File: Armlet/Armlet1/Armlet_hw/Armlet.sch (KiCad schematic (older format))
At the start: 65 parts, among them Q1 NPN, SW1 BUTTON

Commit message: 
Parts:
- removed B? (x3): BAT, symbol BAT
- removed C6: 3.3pF, symbol C
- removed C? (x2): 0.1u, symbol C
- removed C? (x2): 10u, symbol C
- removed D?: D_SHOTTKY, symbol D_SHOTTKY
- removed DA?: NCP1400, symbol NCP1400
- removed DD2: STM32F10X-48, symbol STM32F10X-48
- removed FU?: SOLDERFUSE, symbol SOLDERFUSE
- removed L2, L3, L6, L7: 12nH, 0402, symbol L
- removed L4, L5: 18nH, 0402, symbol L
- removed L?: 22uH, symbol L
- removed R25: 10k, symbol R
- removed RP1, RP2: REFPOINT, symbol REFPOINT
- removed TP2, TP3, TP4: TESTPOINT, symbol TESTPOINT
- removed XL?: CONN_10, symbol CONN_10
- removed XL?: CONN_1, symbol CONN_1
- removed XTAL2: 27MHz, symbol CRYSTAL
- added B1: BAT, BAT_LP383450, symbol BAT
- added C17, C26: 0.1u, symbol C
- added C22, C23: 10u, symbol C
- added C24: 10u, CAP_0805, symbol C
- added C25: 0.1u, CAP_0603, symbol C
- added C27, C28, C29: 1u, symbol C
- added C4: 1.5pF, symbol C
- added D1: 1N4148, SOD323, symbol DIODE
- added DA1: BQ24010, symbol BQ24010
- added DA2: AAT3221, symbol AAT3221
- added DA3: NCP662SQ, symbol NCP662SQ
- added DD2: STM32F100C4, symbol STM32F100C4
- added DD3: M24C02, TSSOP8, symbol EEPROM_I2C
- added R10: 1.5k, symbol R
- added R6: 1.8k*, symbol R
- added R7, R9: 100k, symbol R
- added R8: 3.9k*, symbol R
- added TP1: TESTPOINT, symbol TESTPOINT
- added XL4: USB_MINI_B, symbol USB_MINI_B
- added XTAL1: 26MHz, CRYSTAL, symbol CRYSTAL_H
- C12: renamed from C15; value 18pF -> 10pF
- C13: renamed from C16; value 18pF -> 10pF
- C18: value 0.1u -> 4.7u
- C5: value 1.5pF -> 3.3pF
- gave numbers to parts that had none: 12
- renumbered C12 to C10, C13 to C11, C17 to C14, C4 to C15, C14 to C16, C20 to C19, C8 to C6, C9 to C7, C10 to C8, C11 to C9, Q1 to Q2, R7 to R5, TP5 to TP2, TP1 to TP3
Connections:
- net labels added: +5V, CC_GDO2, CHRG, CHRG_DONE, PB0, PB1, PWR_GOOD, UBat/2
- net labels removed: ADC_BAT, BatteryBtw, Lout, PA12, PB0T3C3, PB1T3C4, PB8, PB9, RX2, TX2
- wire segments 196 -> 229
- no-connect marks 8 -> 9
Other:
- note added: "3.3V 150mA power regulator"
- note added: "I2C Addr = 1010 (A2)(A1)(A0) = 1010 111"
- note added: "L 12nH"
- note added: "L 18nH"
- note added: "Li-Ion charger\n1.5k => 0.56 A"
- note added: "Power"
- note removed: "Solder the fuse \nif no battery installed"
- moved on the sheet: BZ1, C15, C16, C20, C21, M1, Q1, Q2, R2, R3, R4, R5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

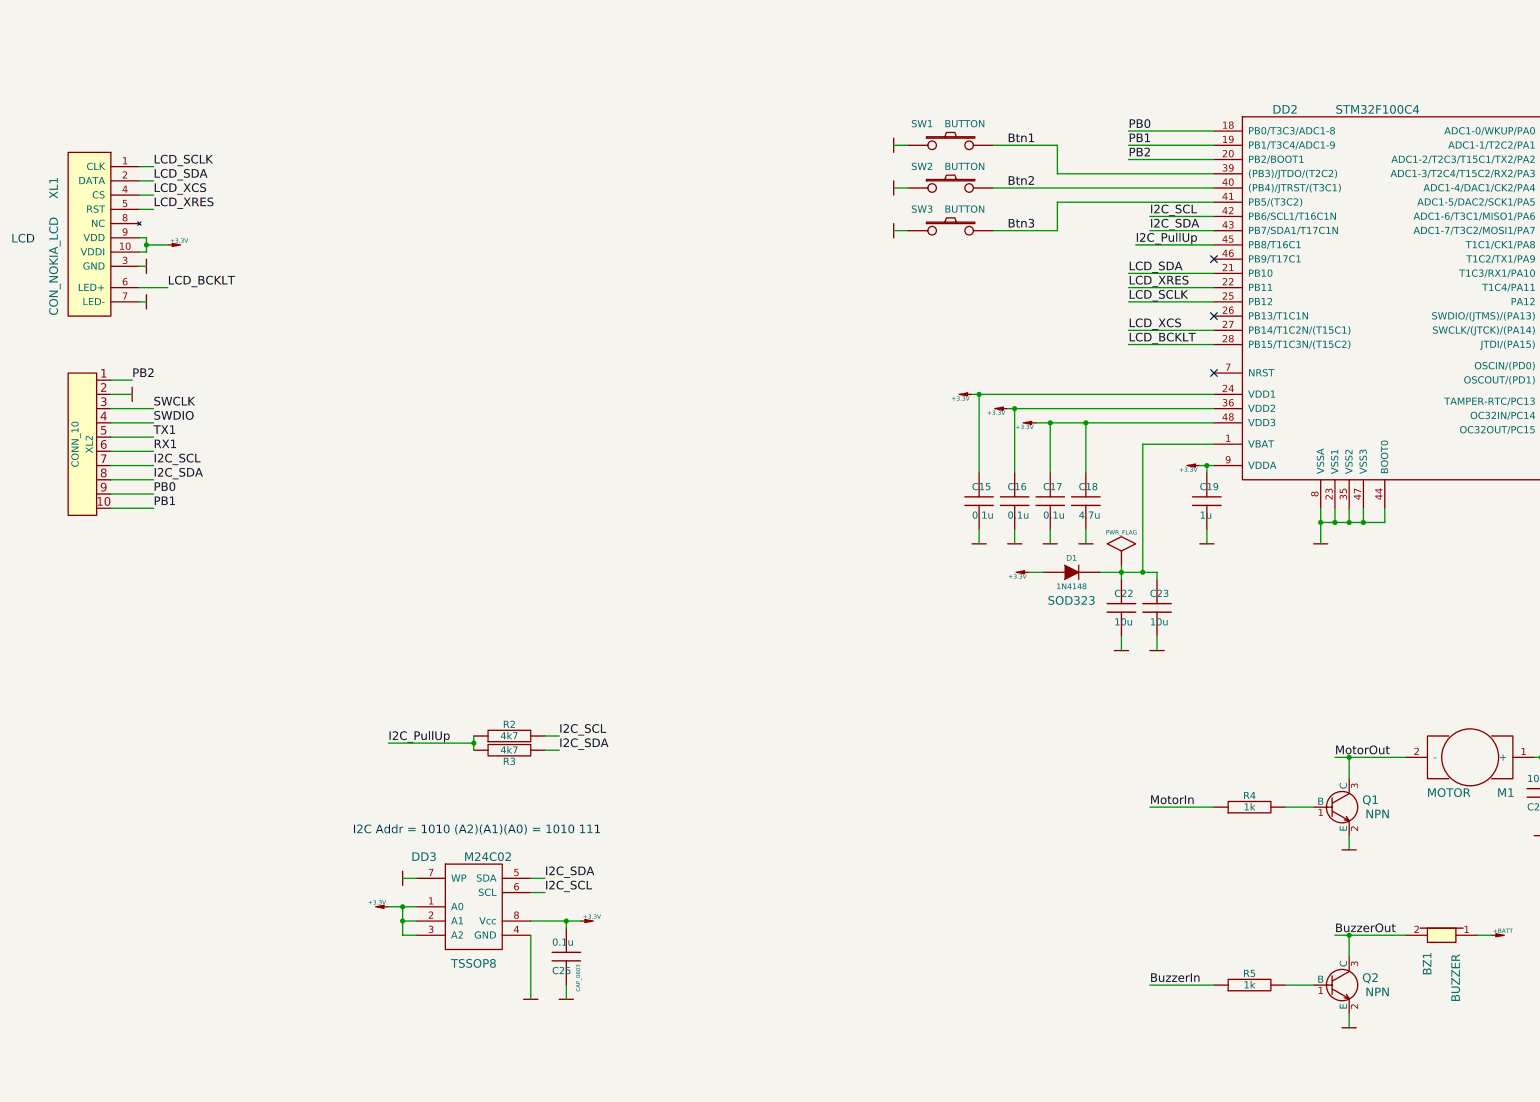
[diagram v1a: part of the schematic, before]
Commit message: 
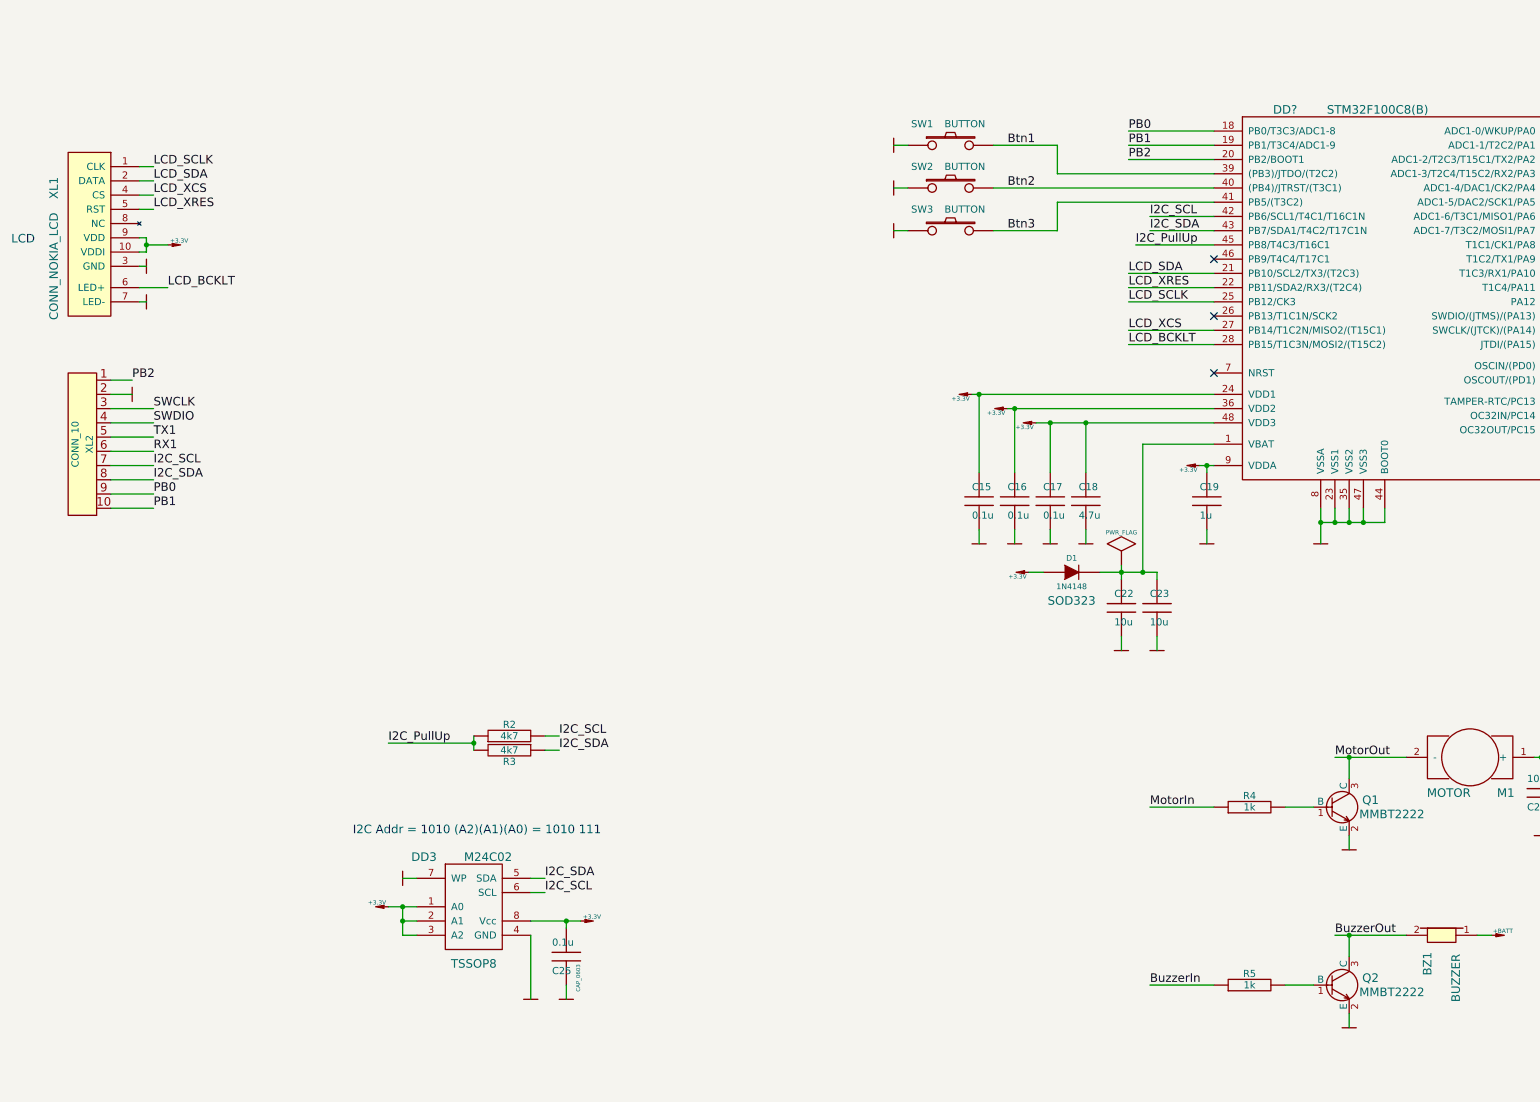
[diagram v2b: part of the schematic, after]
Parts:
- removed DD2: STM32F100C4, symbol STM32F100C4
- removed XL1: CON_NOKIA_LCD, symbol CON_NOKIA_LCD
- added DD?: STM32F100C8(B), symbol STM32F100C8(B)
- added XL1: CONN_NOKIA_LCD, symbol CONN_NOKIA_LCD
- Q1, Q2: value NPN -> MMBT2222
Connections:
- net +3.3V: now also DD?.24 (VDD1), DD?.36 (VDD2), DD?.48 (VDD3), DD?.9 (VDDA), XL1.10 (VDDI), XL1.9 (VDD)
- net Btn1: now also DD?.39 ((PB3)/JTDO/(T2C2))
- net Btn2: now also DD?.40 ((PB4)/JTRST/(T3C1))
- net Btn3: now also DD?.41 (PB5/(T3C2))
- net BuzzerIn: now also DD?.29 (T1C1/CK1/PA8)
- net CC_CS: now also DD?.10 (ADC1-0/WKUP/PA0)
- net CC_GDO0: now also DD?.14 (ADC1-4/DAC1/CK2/PA4)
- net CC_GDO2: now also DD?.13 (ADC1-3/T2C4/T15C2/RX2/PA3)
- net CC_MISO: now also DD?.16 (ADC1-6/T3C1/MISO1/PA6)
- net CC_MOSI: now also DD?.17 (ADC1-7/T3C2/MOSI1/PA7)
- net CC_SCK: now also DD?.15 (ADC1-5/DAC2/SCK1/PA5)
- net CHRG: now also DD?.32 (T1C4/PA11)
- net CHRG_DONE: now also DD?.33 (PA12)
- net GND: now also DD?.23 (VSS1), DD?.35 (VSS2), DD?.44 (BOOT0), DD?.47 (VSS3), DD?.8 (VSSA), XL1.3 (GND), XL1.7 (LED-)
- net I2C_PullUp: now also DD?.45 (PB8/T4C3/T16C1)
- net I2C_SCL: now also DD?.42 (PB6/SCL1/T4C1/T16C1N)
- net I2C_SDA: now also DD?.43 (PB7/SDA1/T4C2/T17C1N)
- net LCD_BCKLT: now also DD?.28 (PB15/T1C3N/MOSI2/(T15C2)), XL1.6 (LED+)
- net LCD_SCLK: now also DD?.25 (PB12/CK3), XL1.1 (CLK)
- net LCD_SDA: now also DD?.21 (PB10/SCL2/TX3/(T2C3)), XL1.2 (DATA)
- net LCD_XCS: now also DD?.27 (PB14/T1C2N/MISO2/(T15C1)), XL1.4 (CS)
- net LCD_XRES: now also DD?.22 (PB11/SDA2/RX3/(T2C4)), XL1.5 (RST)
- net MotorIn: now also DD?.12 (ADC1-2/T2C3/T15C1/TX2/PA2)
- net PB0: now also DD?.18 (PB0/T3C3/ADC1-8)
- net PB1: now also DD?.19 (PB1/T3C4/ADC1-9)
- net PB2: now also DD?.20 (PB2/BOOT1)
- net PWR_GOOD: now also DD?.38 (JTDI/(PA15))
- net RX1: now also DD?.31 (T1C3/RX1/PA10)
- net SWCLK: now also DD?.37 (SWCLK/(JTCK)/(PA14))
- net SWDIO: now also DD?.34 (SWDIO/(JTMS)/(PA13))
- net TX1: now also DD?.30 (T1C2/TX1/PA9)
- net UBat/2: now also DD?.11 (ADC1-1/T2C2/PA1)
- net at C21.1, XTAL2.1: now also DD?.3 (OC32IN/PC14)
- net at C20.1, XTAL2.2: now also DD?.4 (OC32OUT/PC15)
- net at C22.1, C23.1, D1.C: now also DD?.1 (VBAT)
